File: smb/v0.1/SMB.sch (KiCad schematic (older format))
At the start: 38 parts, among them IC1 SP3485CN, IC101 ATMEGA1284-A, J101 RJ45, J102 RTS_RESET, J103 ICSP, J104 SERIAL_REV, P101 I2C_CONN, P102 CONN_3X2, P103 CONN_3X2, P104 CONN_3X2, P105 CONN_5, P106 CONN_3X2, P107 CONN_3, P108 CONN_5, SW101 SKQGAKE010, X101 20MHz

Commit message: correction broche 8 du module RS485 + inversion tx+/tx- au niveau du connecteur + pilotage E/R independant inversion polarit? connecteur d'alim d?placement slot pour rtc simplification routage et optimisation plan de masse (affinage zone exclusion)
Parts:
- removed IC1: SP3485CN, SO8, symbol SP3485CN
- added IC1: MAX485, SO8, symbol MAX485
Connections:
- net labels added: PB1, PC5
- net labels removed: PC7, PD6
- no-connect marks 0 -> 2
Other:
- note added: "UART To RS485"
- moved on the sheet: GS2, GS3, P107, R2, R3, R4

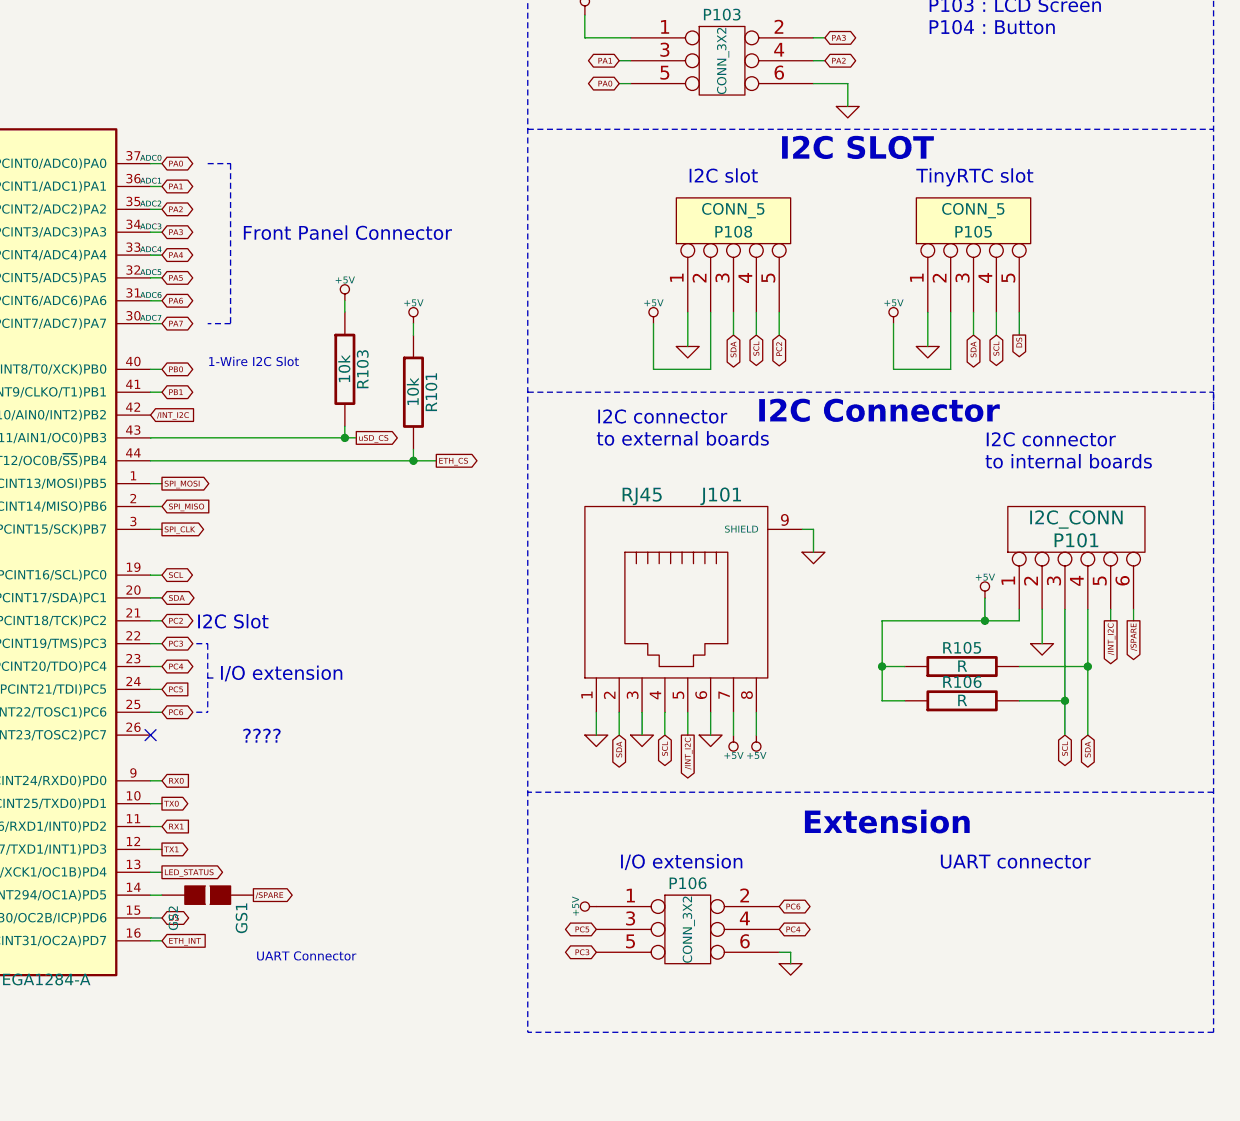
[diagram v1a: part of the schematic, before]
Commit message: correction cablage RJ45 i2c pour etre conforme aux autres cartes 8in8out deplacement de connecteur pour liberer de la place pour les slots
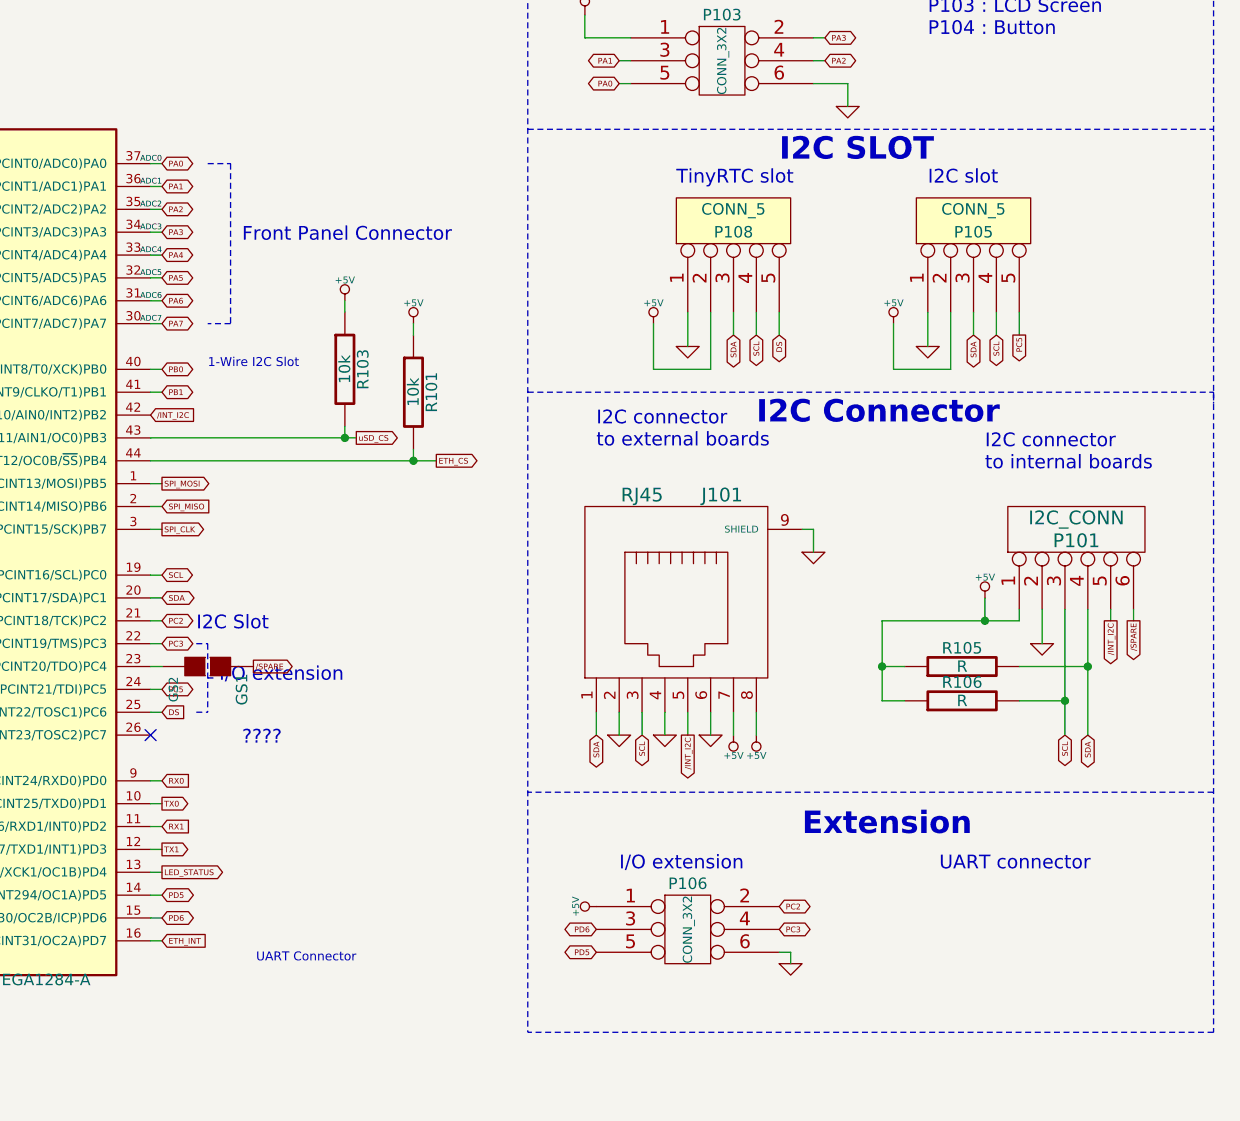
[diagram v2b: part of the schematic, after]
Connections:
- net DS: now also IC101.25 ((PCINT22/TOSC1)PC6), P108.5; no longer IC101.15 ((PCINT30/OC2B/ICP)PD6), P105.5
- net GND: now also J101.2, J101.4; no longer J101.1, J101.3
- net PC2: now also P106.2; no longer P108.5
- net PC3: now also P106.4; no longer P106.5
- net PC5: now also P105.5; no longer P106.3
- net SCL: now also J101.3; no longer J101.4
- net SDA: now also J101.1; no longer J101.2
- net at GS1.2 (G2): now also IC101.23 ((PCINT20/TDO)PC4); no longer IC101.14 ((PCINT294/OC1A)PD5)
- removed net PC4: IC101.23 ((PCINT20/TDO)PC4), P106.4
- removed net PC6: IC101.25 ((PCINT22/TOSC1)PC6), P106.2
- new net PD5: IC101.14 ((PCINT294/OC1A)PD5), P106.5
- new net PD6: IC101.15 ((PCINT30/OC2B/ICP)PD6), P106.3
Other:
- moved on the sheet: GS1
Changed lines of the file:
@@
-EESchema Schematic File Version 2  date mar. 28 mai 2013 22:08:00 CEST
+EESchema Schematic File Version 2  date mar. 04 juin 2013 12:47:30 CEST
 LIBS:power
 LIBS:device
@@
 Sheet 1 4
 Title "Short Main Board - SMB controller"
-Date "28 may 2013"
+Date "4 jun 2013"
 Rev "0"
 Comp "XPLDUINO project"
@@
 Text Label 6500 2550 2    25   ~ 0
 ADC1
-Text GLabel 8700 4950 3    25   BiDi ~ 0
+Text GLabel 8600 4950 3    25   BiDi ~ 0
 SCL
-Text GLabel 8500 4950 3    25   BiDi ~ 0
+Text GLabel 8400 4950 3    25   BiDi ~ 0
 SDA
 Text GLabel 8800 4950 3    25   Output ~ 0
@@
 L GS2 GS1
 U 1 1 503DF9F0
-P 6700 5650
-F 0 "GS1" H 6800 5800 50  0000 C CNN
-F 1 "GS2" H 6800 5501 40  0000 C CNN
-F 2 "" H 6700 5650 60  0001 C CNN
-F 3 "" H 6700 5650 60  0001 C CNN
-	1    6700 5650
+P 6700 4650
+F 0 "GS1" H 6800 4800 50  0000 C CNN
+F 1 "GS2" H 6800 4501 40  0000 C CNN
+F 2 "" H 6700 4650 60  0001 C CNN
+F 3 "" H 6700 4650 60  0001 C CNN
+	1    6700 4650
 	0    1    1    0
 $EndComp
-Text GLabel 6900 5650 2    25   Output ~ 0
+Text GLabel 6900 4650 2    25   Output ~ 0
 /SPARE
 Text GLabel 10750 4450 3    25   Output ~ 0
@@
 Text GLabel 9350 1450 2    25   Output ~ 0
 /RESET
-Text Notes 9800 2550 0    60   ~ 0
+Text Notes 8750 2550 0    60   ~ 0
 TinyRTC slot
 $Comp
@@
 L GND #PWR027
 U 1 1 5191DF48
-P 8400 4950
-F 0 "#PWR027" H 8400 4950 30  0001 C CNN
-F 1 "GND" H 8400 4880 30  0001 C CNN
-F 2 "" H 8400 4950 60  0001 C CNN
-F 3 "" H 8400 4950 60  0001 C CNN
-	1    8400 4950
+P 8500 4950
+F 0 "#PWR027" H 8500 4950 30  0001 C CNN
+F 1 "GND" H 8500 4880 30  0001 C CNN
+F 2 "" H 8500 4950 60  0001 C CNN
+F 3 "" H 8500 4950 60  0001 C CNN
+	1    8500 4950
 	1    0    0    -1
 $EndComp
@@
 L GND #PWR028
 U 1 1 5191DF50
-P 8600 4950
-F 0 "#PWR028" H 8600 4950 30  0001 C CNN
-F 1 "GND" H 8600 4880 30  0001 C CNN
-F 2 "" H 8600 4950 60  0001 C CNN
-F 3 "" H 8600 4950 60  0001 C CNN
-	1    8600 4950
+P 8700 4950
+F 0 "#PWR028" H 8700 4950 30  0001 C CNN
+F 1 "GND" H 8700 4880 30  0001 C CNN
+F 2 "" H 8700 4950 60  0001 C CNN
+F 3 "" H 8700 4950 60  0001 C CNN
+	1    8700 4950
 	1    0    0    -1
 $EndComp
@@
 Text GLabel 6500 4550 2    25   BiDi ~ 0
 PC3
-Text GLabel 6500 4650 2    25   BiDi ~ 0
-PC4
-Text GLabel 6500 4850 2    25   BiDi ~ 0
-PC6
+Text GLabel 6500 4750 2    25   BiDi ~ 0
+PC5
+Text GLabel 6500 5650 2    25   BiDi ~ 0
+PD5
 Wire Wire Line
 	3150 2250 3150 2350
@@
 	6450 4850 6500 4850
 Text GLabel 6500 5750 2    25   BiDi ~ 0
+PD6
+Wire Wire Line
+	6450 5550 6500 5550
+Wire Wire Line
+	6450 5650 6500 5650
+Text GLabel 9200 5800 2    25   BiDi ~ 0
+PC3
+Text GLabel 8400 5900 0    25   BiDi ~ 0
+PD5
+Text GLabel 9200 5700 2    25   BiDi ~ 0
+PC2
+Text GLabel 8400 5800 0    25   BiDi ~ 0
+PD6
+Text GLabel 9200 3200 3    25   BiDi ~ 0
 DS
-Wire Wire Line
-	6450 5550 6500 5550
-Wire Wire Line
-	6450 5650 6500 5650
-Text GLabel 9200 5700 2    25   BiDi ~ 0
-PC6
-Text GLabel 8400 5800 0    25   BiDi ~ 0
-PC5
-Text GLabel 9200 5800 2    25   BiDi ~ 0
-PC4
-Text GLabel 8400 5900 0    25   BiDi ~ 0
-PC3
-Text GLabel 9200 3200 3    25   BiDi ~ 0
-PC2
 Text GLabel 6500 3350 2    25   BiDi ~ 0
 PB0
@@
 Text GLabel 9000 3200 3    25   BiDi ~ 0
 SDA
-Text Notes 8800 2550 0    60   ~ 0
+Text Notes 9850 2550 0    60   ~ 0
 I2C slot
 Wire Wire Line
@@
 Wire Wire Line
 	900  2000 1000 2000
-Text GLabel 6500 4750 2    25   Input ~ 0
+Text GLabel 6500 4850 2    25   Input ~ 0
+DS
+Text GLabel 10250 3200 3    25   Output ~ 0
 PC5
-Text GLabel 10250 3200 3    25   Output ~ 0
-DS
 Wire Wire Line
 	10250 3100 10250 3200

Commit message: ajout gateway onewire DS2482-100 + connecteur 3 points deplacement connecteurs pour amelioration branchement remplacement connecteur 5 points rs485 par 3 points + un strap pour resistance de terminaison
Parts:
- added IC2: DS2482-100S, 1wire-SO08, symbol DS2482-100S
- added P109: CONN_3, symbol CONN_2
- added P110: CONN_3, symbol CONN_3
- added R200: 4.7k, SM0603, symbol R
- P107: symbol CONN_5 -> CONN_3
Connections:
- net +5V: now also IC2.1 (VCC), P110.3 (P3), R200.1
- net GND: now also IC2.3 (GND), IC2.7 (AD1), IC2.8 (AD0), P110.1 (P1)
- net SCL: now also IC2.4 (SCL)
- net SDA: now also IC2.5 (SDA)
- net TX+: now also P109.1 (P1); no longer P107.4
- net at R2.2: now also P109.2 (PM); no longer P107.5
- new net: IC2.2 (1W), P110.2 (PM), R200.2
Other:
- note added: "1-Wire gateway"
- note removed: "1-Wire I2C Slot\n"
- note removed: "????"
- note removed: "I2C Slot"
- note removed: "UART Connector"
- note removed: "UART connector"
- moved on the sheet: C101, C102, C103, C104, C105, C106, GS1, IC101, J101, P101, P102, P103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

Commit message: ajout trou de fixation reprise connecteur 2x10 pour extension deplacement slot I2C ...
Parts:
- removed P104, P106: CONN_3X2, symbol CONN_3X2
- P102: value CONN_3X2 -> CONN_10X2; symbol CONN_3X2 -> CONN_10X2
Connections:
- net +3.3V is gone; now on net +5V: P103.1
- net +5V: now also P102.2 (P2)
- net GND: now also P102.19 (P19), P102.20 (P20); no longer P102.6
- net LED_STATUS: now also P102.6 (P6); no longer P102.2
- net PA4: now also P102.14 (P14)
- net PA5: now also P102.13 (P13)
- net PA6: now also P102.12 (P12)
- net PA7: now also P102.16 (P16)
- net PC2: now also P102.10 (P10)
- net PC3: now also P102.9 (P9)
- net PD5: now also P102.8 (P8)
- net PD6: now also P102.7 (P7)
- net PC7: now reaches IC101.26 ((PCINT23/TOSC2)PC7)
- net PC7: now also P102.11 (P11)
- no-connect marks 2 -> 1
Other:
- note removed: "I/O extension"
- note removed: "P102 : Basic Extension\nP103 : LCD Screen\nP104 : Button"
- moved on the sheet: P103

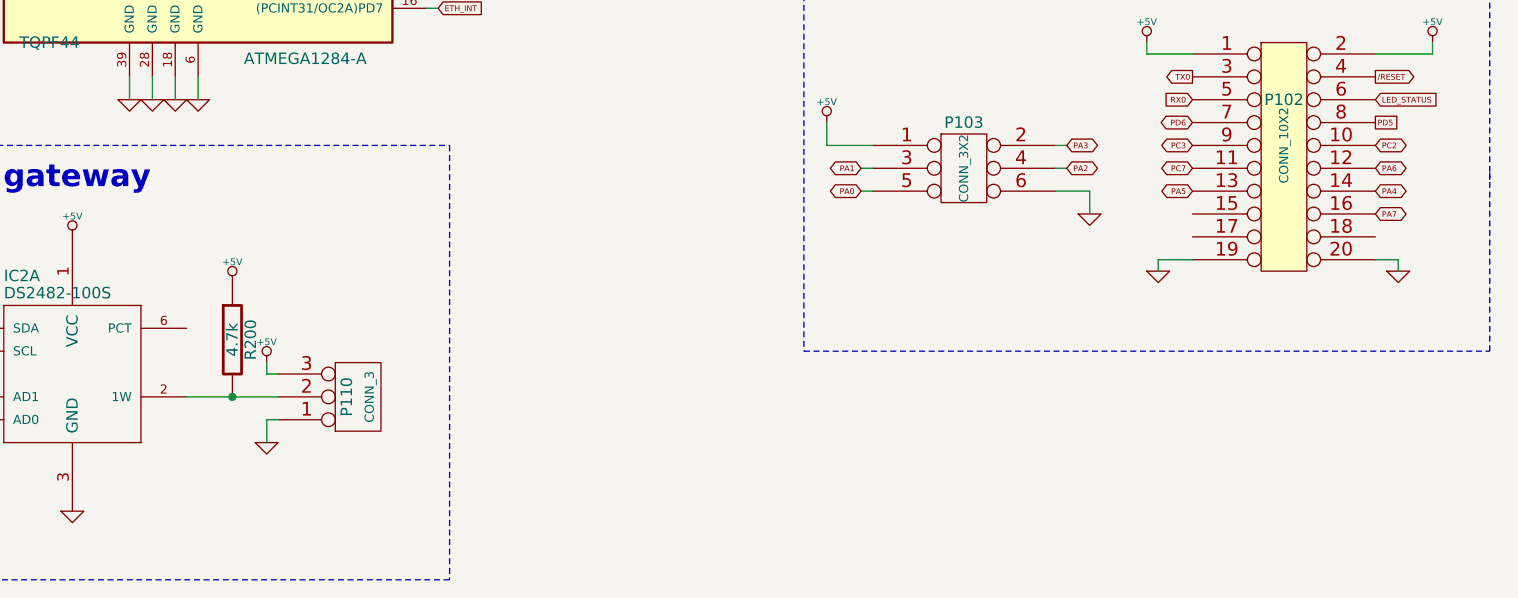
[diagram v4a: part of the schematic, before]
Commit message: generation gerber controle et optimisation routage ajout empreinte TO92 pour ds18b20 ajout i2c sur connecteur d'extension
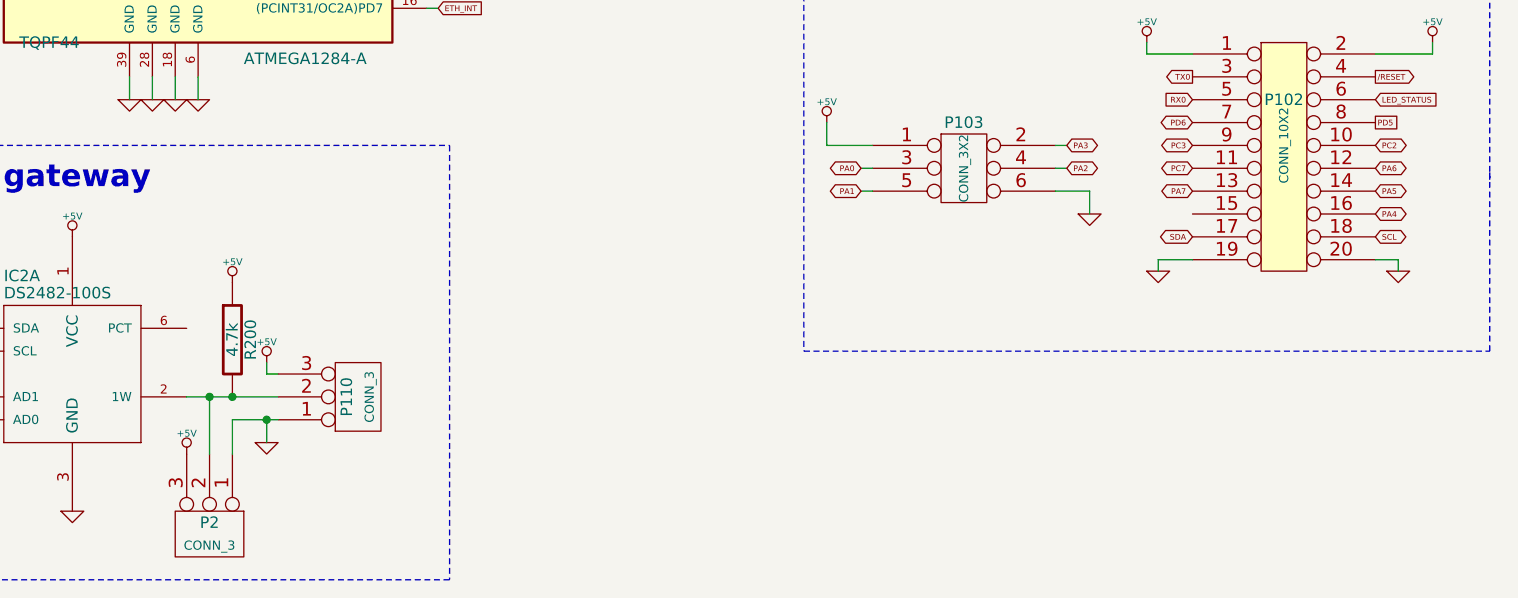
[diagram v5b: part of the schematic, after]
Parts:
- added P2: CONN_3, symbol CONN_3
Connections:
- net +5V: now also P2.3 (P3)
- net GND: now also P2.1 (P1)
- net PA0: now also P103.3; no longer P103.5
- net PA1: now also P103.5; no longer P103.3
- net PA4: now also P102.16 (P16); no longer P102.14 (P14)
- net PA5: now also P102.14 (P14); no longer P102.13 (P13)
- net PA7: now also P102.13 (P13); no longer P102.16 (P16)
- net SCL: now also P102.18 (P18)
- net SDA: now also P102.17 (P17)
- net at IC2.2 (1W), P110.2 (PM), R200.2: now also P2.2 (PM)
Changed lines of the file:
@@
 Text GLabel 9250 5750 2    25   BiDi ~ 0
 PA3
-Text GLabel 8350 5850 0    25   BiDi ~ 0
+Text GLabel 8350 5950 0    25   BiDi ~ 0
 PA1
 Text GLabel 9250 5850 2    25   BiDi ~ 0
 PA2
-Text GLabel 8350 5950 0    25   BiDi ~ 0
+Text GLabel 8350 5850 0    25   BiDi ~ 0
 PA0
-Text GLabel 9800 5950 0    25   BiDi ~ 0
+Text GLabel 10600 5950 2    25   BiDi ~ 0
 PA5
 Text GLabel 10600 5850 2    25   BiDi ~ 0
 PA6
+Text GLabel 9800 5950 0    25   BiDi ~ 0
+PA7
 Text GLabel 10600 6050 2    25   BiDi ~ 0
-PA7
-Text GLabel 10600 5950 2    25   BiDi ~ 0
 PA4
 Text Notes 6850 2100 0    60   ~ 0
@@
 Connection ~ 4150 6950
 Wire Wire Line
-	5800 6950 5750 6950
+	5600 6950 5800 6950
 Wire Wire Line
 	5750 6950 5750 7050
@@
 	11100 6650 11100 5850
 $Comp
-L +5V #PWR?
+L +5V #PWR051
 U 1 1 51BE1AAF
 P 8200 5650
-F 0 "#PWR?" H 8200 5740 20  0001 C CNN
+F 0 "#PWR051" H 8200 5740 20  0001 C CNN
 F 1 "+5V" H 8200 5740 30  0000 C CNN
 F 2 "" H 8200 5650 60  0001 C CNN
@@
 	1    0    0    -1
 $EndComp
+$Comp
+L CONN_3 P2
+U 1 1 51C57E2C
+P 5500 7450
+F 0 "P2" V 5450 7450 50  0000 C CNN
+F 1 "CONN_3" V 5550 7450 40  0000 C CNN
+F 2 "" H 5500 7450 60  0001 C CNN
+F 3 "" H 5500 7450 60  0001 C CNN
+	1    5500 7450
+	0    1    1    0
+$EndComp
+Wire Wire Line
+	5500 6850 5500 7100
+Connection ~ 5500 6850
+Wire Wire Line
+	5600 6950 5600 7100
+Connection ~ 5750 6950
+$Comp
+L +5V #PWR052
+U 1 1 51C581D7
+P 5400 7100
+F 0 "#PWR052" H 5400 7190 20  0001 C CNN
+F 1 "+5V" H 5400 7190 30  0000 C CNN
+F 2 "" H 5400 7100 60  0000 C CNN
+F 3 "" H 5400 7100 60  0000 C CNN
+	1    5400 7100
+	1    0    0    -1
+$EndComp
+Text GLabel 9800 6150 0    25   BiDi ~ 0
+SDA
+Text GLabel 10600 6150 2    25   BiDi ~ 0
+SCL
 $EndSCHEMATC
